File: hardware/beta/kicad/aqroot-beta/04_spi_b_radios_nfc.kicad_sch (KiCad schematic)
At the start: 10 parts, among them U7 CC1101_RADIO_PLACEHOLDER, U8 SX1262_MODULE_PLACEHOLDER, U9 ST25R3916_NFC_PLACEHOLDER

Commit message: AQROOT Beta: assign standard passive footprints
Assigns footprints to 40 passives whose package is unambiguous from
existing project precedent. Property-value edits only - no symbol, wire,
label or net touched.

  28 resistors -> Resistor_SMD:R_0603_1608Metric
     R1 R2 R3-R17 R18 R19 R20 R21 R22 R23 R25 R26 R27 R28 R29
     Basis: all 39 already-assigned resistors in the project are 0603, and
     every one of these is signal-level (pull-ups, dividers, series
     termination, MOSFET gate network).

  12 capacitors -> Capacitor_SMD:C_0603_1608Metric
     C1 C2 C4 C5 C6 C7 C8 C9 C13 C14 C16 C17
     Basis: 100nF is 5/5 and 1uF is 4/4 for 0603 among already-assigned
     capacitors - unanimous.

DELIBERATELY NOT ASSIGNED - split precedent, needs a decision:
  C3, C15, C10  10uF   -> project uses BOTH C_1206 (x2) and C_0805 (x1)
  C11           4.7uF  -> single 0805 precedent, different subsystem
Bulk capacitors must not be blindly converted to 0603, and the existing
precedent does not settle 0805 vs 1206.

Also untouched per instruction: C12/R24/Q1 (TBD), C18/C19 (placeholder),
L1/L2, mechanical switches and connectors, and the four RF/module
placeholders.

Separately noted, NOT changed here: C24 is 22uF 25V X7R with
C_0603_1608Metric already assigned. A 22uF 25V X7R does not exist in 0603
and the project's other 22uF parts use 1206/0805 - this looks like a
pre-existing error and is flagged for the BOM pass, not silently altered.

Verified with kicad-cli: netlist pin-to-net mapping byte-identical before
and after. ERC unchanged: raw 48, unique 24, excluded 24, real 0.
Footprint coverage 97 -> 137 of 166 components.

Co-Authored-By: Claude Opus 5 <noreply@anthropic.com>
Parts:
- C16, C17: footprint (none) -> Capacitor_SMD:C_0603_1608Metric
- R27, R28, R29: footprint (none) -> Resistor_SMD:R_0603_1608Metric
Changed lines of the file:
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@@
 			)
 		)
-		(property "Footprint" ""
+		(property "Footprint" "Resistor_SMD:R_0603_1608Metric"
 			(at 264.922 99.06 90)
 			(hide yes)
@@
 			)
 		)
-		(property "Footprint" ""
+		(property "Footprint" "Resistor_SMD:R_0603_1608Metric"
 			(at 141.732 74.93 90)
 			(hide yes)
@@
 			)
 		)
-		(property "Footprint" ""
+		(property "Footprint" "Capacitor_SMD:C_0603_1608Metric"
 			(at 257.5052 81.28 0)
 			(hide yes)
@@
 			)
 		)
-		(property "Footprint" ""
+		(property "Footprint" "Capacitor_SMD:C_0603_1608Metric"
 			(at 127.9652 78.74 0)
 			(hide yes)
@@
 			)
 		)
-		(property "Footprint" ""
+		(property "Footprint" "Resistor_SMD:R_0603_1608Metric"
 			(at 140.462 157.48 90)
 			(hide yes)

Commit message: Close metadata drift on SW9, U7, U8, U9, J3; verify netlist and ERC unchanged
Five symbols carried metadata contradicting decisions already locked elsewhere
in the Design Decisions Log. No external vendor document was needed for any of
them - this propagates existing locks rather than selecting anything new.

SW9 - the Note still declared an unresolved SPST/SPDT symbol conflict and said
the symbol change "was NOT made here". That is stale: the instance is already
Switch:SW_SPDT with pins 1/2/3. Pole mapping is now VERIFIED 1:1 - the KiCad
symbol places pin 2 (name B) alone at (-5.08, 0), opposite throws 1 (A) and
3 (C), which is what makes it the pole, and C&K terminal 2 is likewise the
COMMON/POLE, so no cross-map is needed. Netlist confirms pin 2 to BQ25185_SYS,
pin 1 to U12 EN and TP13, pin 3 an unused throw carrying a no_connect.
Electrical intent unchanged, still SPST-in-practice. SW9 is no longer blocked on
symbol numbering - only on land-pattern geometry from the C&K layout drawing.

U7/U8 - both still read Manufacturer TBD, MPN TBD despite the RF plan locking
the Ebyte modules. U7 is now Ebyte E07-400M10S (433 MHz, CC1101) and U8 is Ebyte
E22-900M22S (915 MHz, SX1262). Their Package fields also record the standing
constraint that each module owns its matching network and presents a matched
50-ohm IPEX port, so no matching network and no separate U.FL test connector
belong on the main PCB. Footprints remain blocked pending Ebyte drawings.

U9 - MPN was still bare ST25R3916. The NFC package lock explicitly closed that
open question, so the suffix is now recorded: ST25R3916-AQET, VQFN-32 5x5 mm,
discrete and not a plug-on module. Footprint still blocked pending ST's outline.

J3 - had a GCT-specific footprint but no Manufacturer and no MPN property at
all. Added GCT and USB4105-GF-A-120, with the Package field stating plainly that
the family is locked while the variant suffix remains a CANDIDATE, unconfirmed
against the GCT drawing at the locked 1.6 mm board th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
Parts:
- U7: MPN TBD -> E07-400M10S; Manufacturer TBD -> Ebyte (Chengdu Ebyte Electronic Technology); Package (none) -> Certified CC1101-based 433 MHz SMD module with on-board RF 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
- U8: MPN TBD -> E22-900M22S; Manufacturer TBD -> Ebyte (Chengdu Ebyte Electronic Technology); Package (none) -> Certified SX1262-based 915 MHz SMD module with on-board RF 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
- U9: MPN ST25R3916 -> ST25R3916-AQET; Package (none) -> VQFN-32 (5x5 mm), discrete NFC front-end - part AND package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
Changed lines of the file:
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@@
 			)
 		)
-		(property "MPN" "ST25R3916"
+		(property "MPN" "ST25R3916-AQET"
+			(at 91.44 143.51 0)
+			(hide yes)
+			(show_name no)
+			(do_not_autoplace no)
+			(effects
+				(font
+					(size 1.27 1.27)
+				)
+			)
+		)
+		(property "Package" "VQFN-32 (5x5 mm), discrete NFC front-end - part AND package LOCKED per 'NFC package LOCKED: ST25R3916-AQET'. NOT a plug-on NFC module. Footprint BLOCKED: needs the official ST package outline / recommended footprint. VDD_PA runs from the switched 5V boost; VDD_IO REMAINS +3V3."
 			(at 91.44 143.51 0)
 			(hide yes)
@@
 			)
 		)
-		(property "Manufacturer" "TBD"
+		(property "Manufacturer" "Ebyte (Chengdu Ebyte Electronic Technology)"
 			(at 217.17 63.5 0)
 			(hide yes)
@@
 			)
 		)
-		(property "MPN" "TBD"
+		(property "MPN" "E22-900M22S"
+			(at 217.17 63.5 0)
+			(hide yes)
+			(show_name no)
+			(do_not_autoplace no)
+			(effects
+				(font
+					(size 1.27 1.27)
+				)
+			)
+		)
+		(property "Package" "Certified SX1262-based 915 MHz SMD module with on-board RF front-end and IPEX/u.FL port - part LOCKED per '12 - RF and Antenna Plan'. Footprint BLOCKED: needs the official Ebyte E22-900M22S mechanical drawing / recommended land pattern. The module owns its matching network; NO 915 MHz matching network or U.FL test connector belongs on the main PCB."
 			(at 217.17 63.5 0)
 			(hide yes)
@@
 			)
 		)
-		(property "Manufacturer" "TBD"
+		(property "Manufacturer" "Ebyte (Chengdu Ebyte Electronic Technology)"
 			(at 87.63 57.15 0)
 			(hide yes)
@@
 			)
 		)
-		(property "MPN" "TBD"
+		(property "MPN" "E07-400M10S"
 			(at 87.63 57.15 0)
 			(hide yes)
+			(show_name no)
+			(do_not_autoplace no)
+			(effects
+				(font
+					(size 1.27 1.27)
+				)
+			)
+		)
+		(property "Package" "Certified CC1101-based 433 MHz SMD module with on-board RF front-end and IPEX/u.FL port - part LOCKED per '12 - RF and Antenna Plan'. Footprint BLOCKED: needs the official Ebyte E07-400M10S mechanical drawing / recommended land pattern. The module owns its matching network; NO 433 MHz matching network or U.FL test connector belongs on the main PCB."
+			(at 87.63 57.15 0)
+			(hide yes)

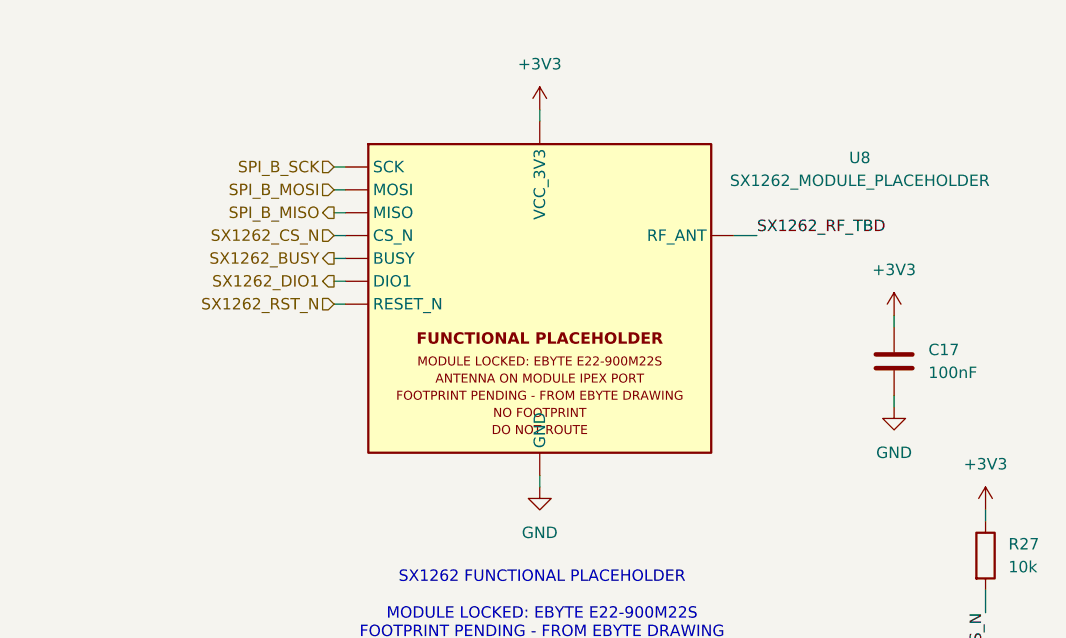
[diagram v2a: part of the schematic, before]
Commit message: AQROOT Beta: integrate E22 module and dedicate XGPIO14 to RX control
Atomic change across four files - root, sheet 04, sheet 08 and sheet 09 -
because the hierarchy reallocation and the module capture are electrically
coupled and neither is valid alone.

APPLIED TO U8, NOT U7. The schematic is authoritative: U8 is the SX1262 /
E22-900M22S at 915 MHz and U7 remains the CC1101 / E07-400M10S at 433 MHz. The
earlier blocker-register transposition is corrected and annotated in the log;
U7 is untouched and still a placeholder awaiting its own vendor audit.

U8 CAPTURE. The SX1262_MODULE_PLACEHOLDER is replaced by the physical 22-pin
E22-900M22S symbol on AQROOT_Beta:Ebyte_E22-900M22S. All 22 pads resolve, none
unconnected: the ten physical grounds - pins 1 to 5, 10, 11, 12, 20 and 22 - all
land on GND individually rather than being collapsed, pin 9 VCC is on +3V3, and
pins 13 to 19 carry SX1262_DIO1, SX1262_BUSY, SX1262_RST_N, SPI_B_MISO,
SPI_B_MOSI, SPI_B_SCK and SX1262_CS_N respectively. The seven existing
hierarchical labels were relocated onto the new pin stubs rather than
duplicated.

RF SWITCH. DIO2 on pin 8 is strapped locally to TXEN on pin 7, and the netlist
confirms DIO2_TXEN contains exactly those two nodes and nothing else, so no MCU
or expander pin is consumed for transmit control. Firmware must enable
SetDIO2AsRfSwitchCtrl or TXEN never asserts. Receive control comes from
SX1262_RXEN, which contains exactly U3 pin 19, U8 pin 6 and the new R74
pulldown.

XGPIO14 RETIRED. U3 pin 19 is reallocated from XGPIO14 to SX1262_RXEN across the
whole hierarchy - the sheet 08 hierarchical label, the sheet 08 sheet pin in the
root, and a new sheet 04 sheet pin plus root label. On sheet 09 the community
path is removed: R65 and its wires are deleted, the XGPIO14 hierarchical label
is gone, and both XGPIO14_HDR labels become RESERVED_NC, so J5 pin 19 no longer
advertises a GPIO. D6's now-spare ESD channel carries an explicit no_connect.
XGPIO0 to XGPIO13 are untouched and a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
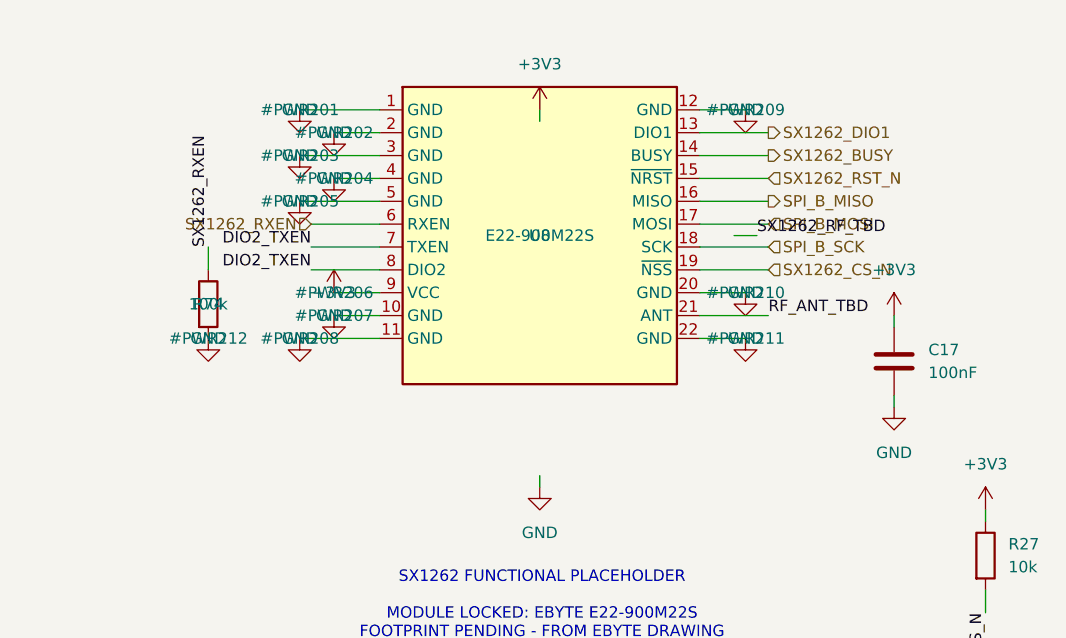
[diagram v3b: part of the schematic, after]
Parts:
- removed U8: SX1262_MODULE_PLACEHOLDER, symbol AQROOT_Beta:SX1262_MODULE_PLACEHOLDER
- added R74: 100k, Resistor_SMD:R_0603_1608Metric, symbol Device:R
- added U8: E22-900M22S, AQROOT_Beta:Ebyte_E22-900M22S, symbol AQROOT_Beta:E22-900M22S
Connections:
- net +3V3: now also U8.9 (VCC)
- net GND: now also R74.2, U8.1 (GND), U8.10 (GND), U8.11 (GND), U8.12 (GND), U8.2 (GND), U8.20 (GND), U8.22 (GND), U8.3 (GND), U8.4 (GND), U8.5 (GND)
- net SPI_B_MISO: now also U8.16 (MISO)
- net SPI_B_MOSI: now also U8.17 (MOSI)
- net SPI_B_SCK: now also U8.18 (SCK)
- net SX1262_BUSY: now also U8.14 (BUSY)
- net SX1262_CS_N: now also U8.19 (~{NSS})
- net SX1262_DIO1: now also U8.13 (DIO1)
- net SX1262_RST_N: now also U8.15 (~{NRST})
- new net DIO2_TXEN: U8.7 (TXEN), U8.8 (DIO2)
- new net RF_ANT_TBD: U8.21 (ANT)
- new net SX1262_RXEN: R74.1, U8.6 (RXEN)

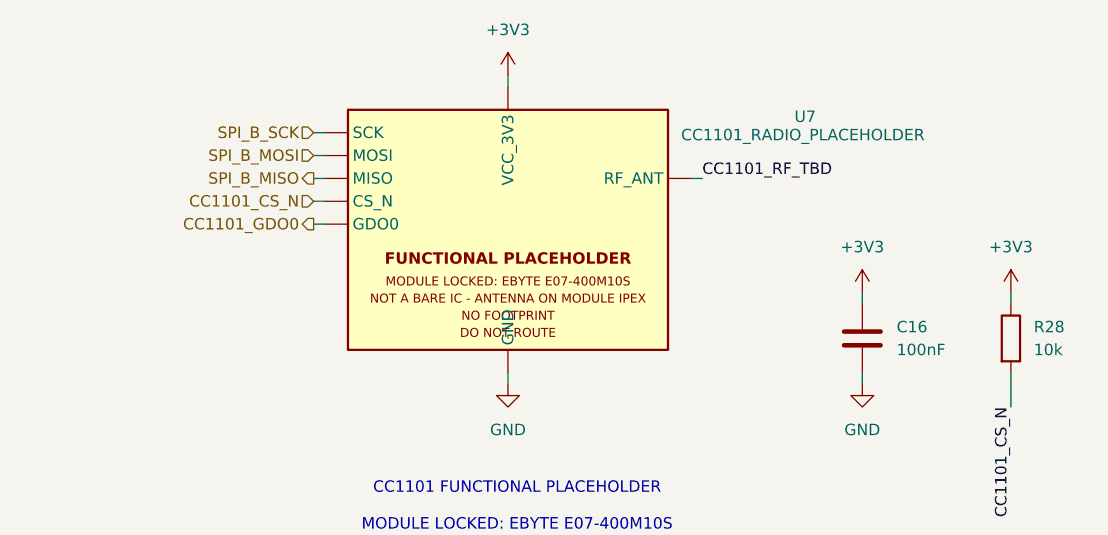
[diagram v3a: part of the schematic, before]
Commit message: AQROOT Beta: integrate physical CC1101 module
Replaces the CC1101_RADIO_PLACEHOLDER at U7 with the physical 22-pin
E07-400M10S symbol on AQROOT_Beta:Ebyte_E07-400M10S. Single sheet touched,
04_spi_b_radios_nfc.

All 22 pads accounted for. The nine physical grounds - pins 1 to 5, 11, 12, 20
and 22 - each resolve to GND individually rather than being collapsed, pin 9
VCC is on +3V3, and pins 15 to 19 carry CC1101_GDO0, SPI_B_MISO, SPI_B_MOSI,
SPI_B_SCK and CC1101_CS_N respectively. The five existing hierarchical labels
were relocated onto the new pin stubs rather than duplicated. Note pin 16 is
MISO multiplexed with GDO1 on this module, so the single pad serves both.

GDO2 IS INTENTIONALLY UNCONNECTED, on vendor authority rather than assumption.
The manual states GDO2 is generally configured as an IRQ-like function but may
also be left unconnected, with interrupt status obtainable by SPI polling,
while noting an MCU external interrupt is recommended. AQROOT allocates no GPIO
for it - the native budget is closed and both expanders are full - so pin 14
carries an explicit no_connect flag. No GPIO was invented for it and no
MCU pin mapping changed.

Pins 6, 7, 8, 10 and 13 are vendor NC, described in the manual as needing no
connection. They are typed no_connect in the symbol and left bare, so they are
physically represented for 1:1 footprint verification without generating ERC
noise.

ANTENNA. Pin 21 ANT is represented on the named net CC1101_ANT_TBD, distinct
from the E22 RF_ANT_TBD so the two RF pads cannot merge, and is deliberately
not routed. Beta uses the module IPEX/u.FL path with the Taoglas
FXP450.07.0100C for 433 MHz, pairing that is unchanged. Procurement must
confirm delivered units have the IPEX connector populated. RF DO NOT ROUTE
stands.

VALIDATION. Netlist 158 to 159 nets, the single addition being CC1101_ANT_TBD,
and the set of changed nets not involving U7 is EMPTY. SPI bus B correctly
carries U1, U7 and U8 on all three of SCK, MOSI and MISO. CC1101_C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
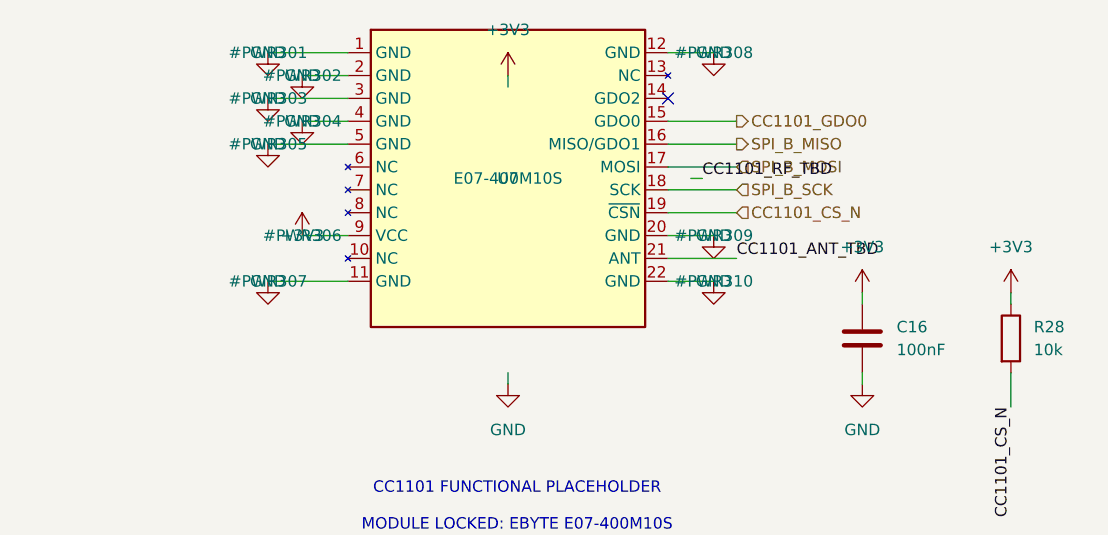
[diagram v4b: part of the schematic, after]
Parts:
- removed U7: CC1101_RADIO_PLACEHOLDER, symbol AQROOT_Beta:CC1101_RADIO_PLACEHOLDER
- added U7: E07-400M10S, AQROOT_Beta:Ebyte_E07-400M10S, symbol AQROOT_Beta:E07-400M10S
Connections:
- net +3V3: now also U7.9 (VCC)
- net CC1101_CS_N: now also U7.19 (~{CSN})
- net CC1101_GDO0: now also U7.15 (GDO0)
- net GND: now also U7.1 (GND), U7.11 (GND), U7.12 (GND), U7.2 (GND), U7.20 (GND), U7.22 (GND), U7.3 (GND), U7.4 (GND), U7.5 (GND)
- net SPI_B_MISO: now also U7.16 (MISO/GDO1)
- net SPI_B_MOSI: now also U7.17 (MOSI)
- net SPI_B_SCK: now also U7.18 (SCK)
- new net CC1101_ANT_TBD: U7.21 (ANT)
- no-connect marks 0 -> 1
